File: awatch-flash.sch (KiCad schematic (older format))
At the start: 3 parts

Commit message: annotate all
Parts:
- gave numbers to parts that had none: 3
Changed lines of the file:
@@
 $EndDescr
 $Comp
-L awatch-parts:W25Q128JV U?
+L awatch-parts:W25Q128JV U401
 U 1 1 5C3CBD41
 P 4850 3500
-F 0 "U?" H 5000 2700 50  0000 C CNN
+F 0 "U401" H 5000 2700 50  0000 C CNN
 F 1 "W25Q128JV" H 5500 2700 50  0000 C CNN
 F 2 "" H 4850 3500 50  0001 C CNN
@@
 FLASH_D3
 $Comp
-L power:GND #PWR?
+L power:GND #PWR0135
 U 1 1 5C3CBF2A
 P 5250 4450
-F 0 "#PWR?" H 5250 4200 50  0001 C CNN
+F 0 "#PWR0135" H 5250 4200 50  0001 C CNN
 F 1 "GND" H 5255 4277 50  0000 C CNN
 F 2 "" H 5250 4450 50  0001 C CNN
@@
 	5250 4450 5250 4350
 $Comp
-L power:+2V8 #PWR?
+L power:+2V8 #PWR0136
 U 1 1 5C3CBFA2
 P 5250 3300
-F 0 "#PWR?" H 5250 3150 50  0001 C CNN
+F 0 "#PWR0136" H 5250 3150 50  0001 C CNN
 F 1 "+2V8" H 5265 3473 50  0000 C CNN
 F 2 "" H 5250 3300 50  0001 C CNN
@@
 	5250 3300 5250 3400
 $Comp
-L power:+2V8 #PWR?
+L power:+2V8 #PWR0137
 U 1 1 5C3CC024
 P 3200 3500
-F 0 "#PWR?" H 3200 3350 50  0001 C CNN
+F 0 "#PWR0137" H 3200 3350 50  0001 C CNN
 F 1 "+2V8" H 3215 3673 50  0000 C CNN
 F 2 "" H 3200 3500 50  0001 C CNN
@@
 $EndComp
 $Comp
-L power:GND #PWR?
+L power:GND #PWR0138
 U 1 1 5C3CC033
 P 3200 4250
-F 0 "#PWR?" H 3200 4000 50  0001 C CNN
+F 0 "#PWR0138" H 3200 4000 50  0001 C CNN
 F 1 "GND" H 3205 4077 50  0000 C CNN
 F 2 "" H 3200 4250 50  0001 C CNN
@@
 $EndComp
 $Comp
-L Device:C_Small C?
+L Device:C_Small C401
 U 1 1 5C3CC05F
 P 3200 3850
-F 0 "C?" H 3292 3896 50  0000 L CNN
+F 0 "C401" H 3292 3896 50  0000 L CNN
 F 1 "1µF" H 3292 3805 50  0000 L CNN
 F 2 "" H 3200 3850 50  0001 C CNN
@@
 	3200 3950 3200 4000
 $Comp
-L Device:C_Small C?
+L Device:C_Small C402
 U 1 1 5C3CC16A
 P 3600 3850
-F 0 "C?" H 3692 3896 50  0000 L CNN
+F 0 "C402" H 3692 3896 50  0000 L CNN
 F 1 "0.1µF" H 3692 3805 50  0000 L CNN
 F 2 "" H 3600 3850 50  0001 C CNN

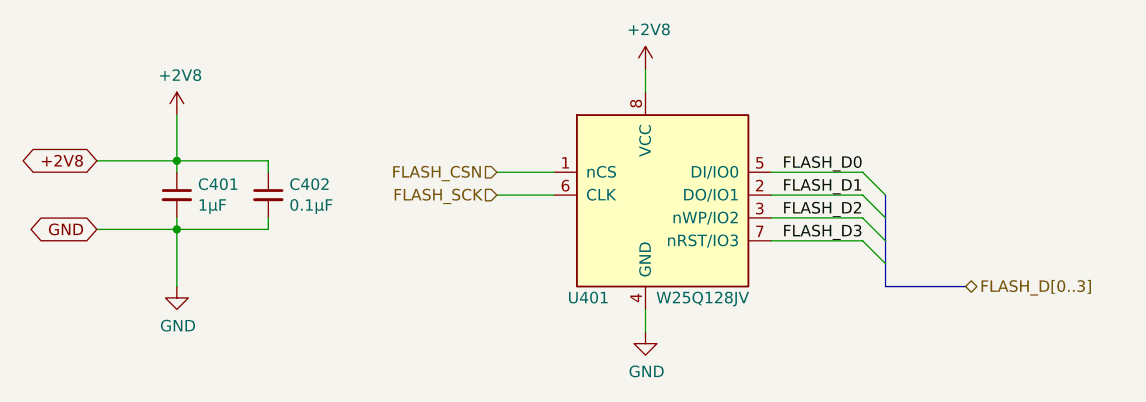
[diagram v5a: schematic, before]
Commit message: Add footprints.
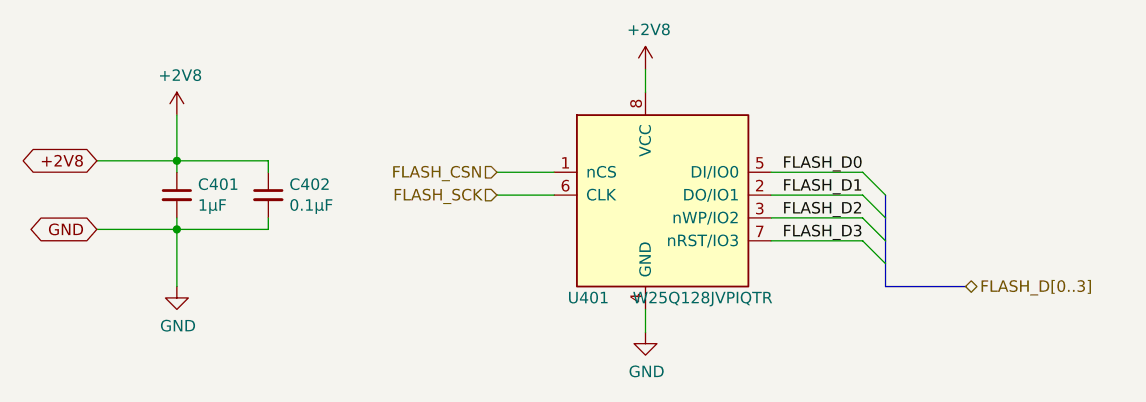
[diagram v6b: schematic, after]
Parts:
- C401, C402: footprint (none) -> Capacitor_SMD:C_0603_1608Metric
- U401: value W25Q128JV -> W25Q128JVPIQTR; footprint (none) -> Package_SON:WSON-8-1EP_6x5mm_P1.27mm_EP3.4x4mm
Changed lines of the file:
@@
 EESchema Schematic File Version 4
+LIBS:awatch2-cache
 EELAYER 26 0
 EELAYER END
@@
 P 4850 3500
 F 0 "U401" H 5000 2700 50  0000 C CNN
-F 1 "W25Q128JV" H 5500 2700 50  0000 C CNN
-F 2 "" H 4850 3500 50  0001 C CNN
+F 1 "W25Q128JVPIQTR" H 5500 2700 50  0000 C CNN
+F 2 "Package_SON:WSON-8-1EP_6x5mm_P1.27mm_EP3.4x4mm" H 4850 3500 50  0001 C CNN
 F 3 "" H 4850 3500 50  0001 C CNN
 	1    4850 3500
@@
 F 0 "C401" H 3292 3896 50  0000 L CNN
 F 1 "1µF" H 3292 3805 50  0000 L CNN
-F 2 "" H 3200 3850 50  0001 C CNN
+F 2 "Capacitor_SMD:C_0603_1608Metric" H 3200 3850 50  0001 C CNN
 F 3 "~" H 3200 3850 50  0001 C CNN
 	1    3200 3850
@@
 F 0 "C402" H 3692 3896 50  0000 L CNN
 F 1 "0.1µF" H 3692 3805 50  0000 L CNN
-F 2 "" H 3600 3850 50  0001 C CNN
+F 2 "Capacitor_SMD:C_0603_1608Metric" H 3600 3850 50  0001 C CNN
 F 3 "~" H 3600 3850 50  0001 C CNN
 	1    3600 3850

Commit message: approx. final layout
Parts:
- C401: value 1µF -> 1.0µF X7R; DigiKey PN (none) -> 1276-1946-1-ND
- C402: value 0.1µF -> 0.1µF X7R; DigiKey PN (none) -> 1276-1061-1-ND
- U401: DigiKey PN (none) -> W25Q128JVPIQCT-ND
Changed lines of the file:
@@
 $Descr A4 11693 8268
 encoding utf-8
-Sheet 4 9
+Sheet 4 10
 Title "AWatch2"
 Date ""
@@
 F 2 "Package_SON:WSON-8-1EP_6x5mm_P1.27mm_EP3.4x4mm" H 4850 3500 50  0001 C CNN
 F 3 "" H 4850 3500 50  0001 C CNN
+F 4 "W25Q128JVPIQCT-ND" H 0   0   50  0001 C CNN "DigiKey PN"
 	1    4850 3500
 	1    0    0    -1
@@
 P 3200 3850
 F 0 "C401" H 3292 3896 50  0000 L CNN
-F 1 "1µF" H 3292 3805 50  0000 L CNN
+F 1 "1.0µF X7R" H 3292 3805 50  0000 L CNN
 F 2 "Capacitor_SMD:C_0603_1608Metric" H 3200 3850 50  0001 C CNN
 F 3 "~" H 3200 3850 50  0001 C CNN
+F 4 "1276-1946-1-ND" H 0   0   50  0001 C CNN "DigiKey PN"
 	1    3200 3850
 	1    0    0    -1
@@
 P 3600 3850
 F 0 "C402" H 3692 3896 50  0000 L CNN
-F 1 "0.1µF" H 3692 3805 50  0000 L CNN
+F 1 "0.1µF X7R" H 3692 3805 50  0000 L CNN
 F 2 "Capacitor_SMD:C_0603_1608Metric" H 3600 3850 50  0001 C CNN
 F 3 "~" H 3600 3850 50  0001 C CNN
+F 4 "1276-1061-1-ND" H 0   0   50  0001 C CNN "DigiKey PN"
 	1    3600 3850
 	1    0    0    -1
